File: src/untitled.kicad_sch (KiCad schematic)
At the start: 45 parts, among them J4 Conn_02x15_Odd_Even, J5 USB_C_Receptacle_USB2.0_14P, U4 W25Q128JVS, U5 NCP1117-1.5_SOT223, Y2 ABM8-272-T3

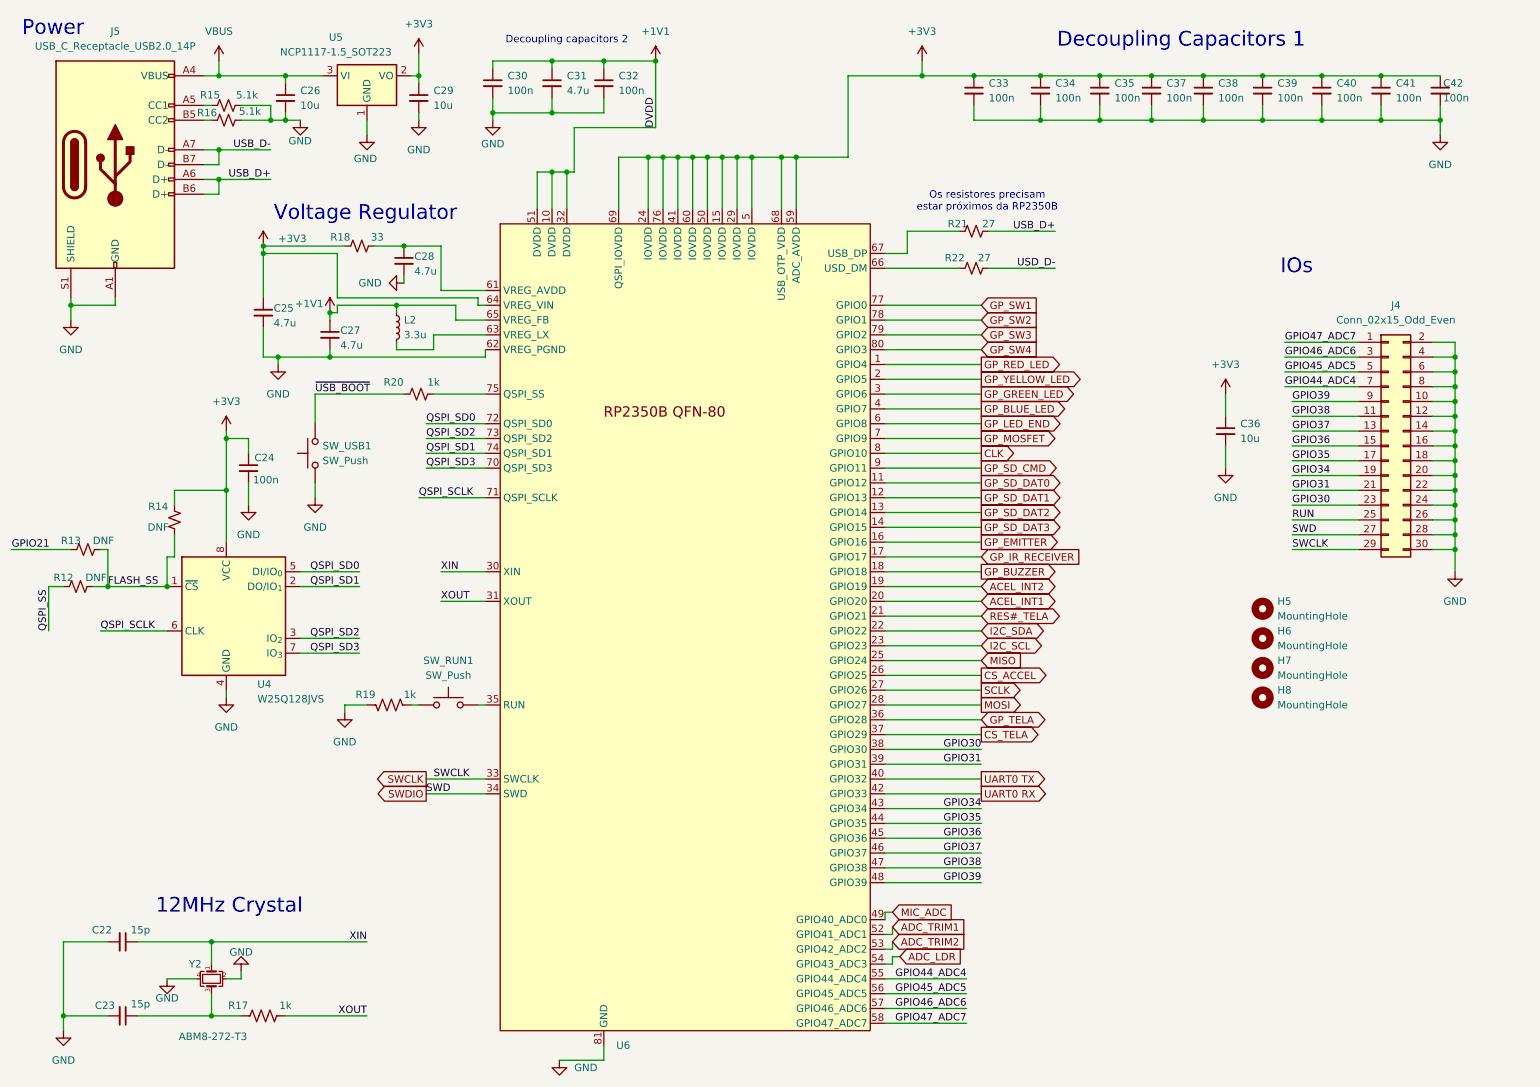
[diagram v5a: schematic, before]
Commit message: adicionado footprints, falta microfone e display somente
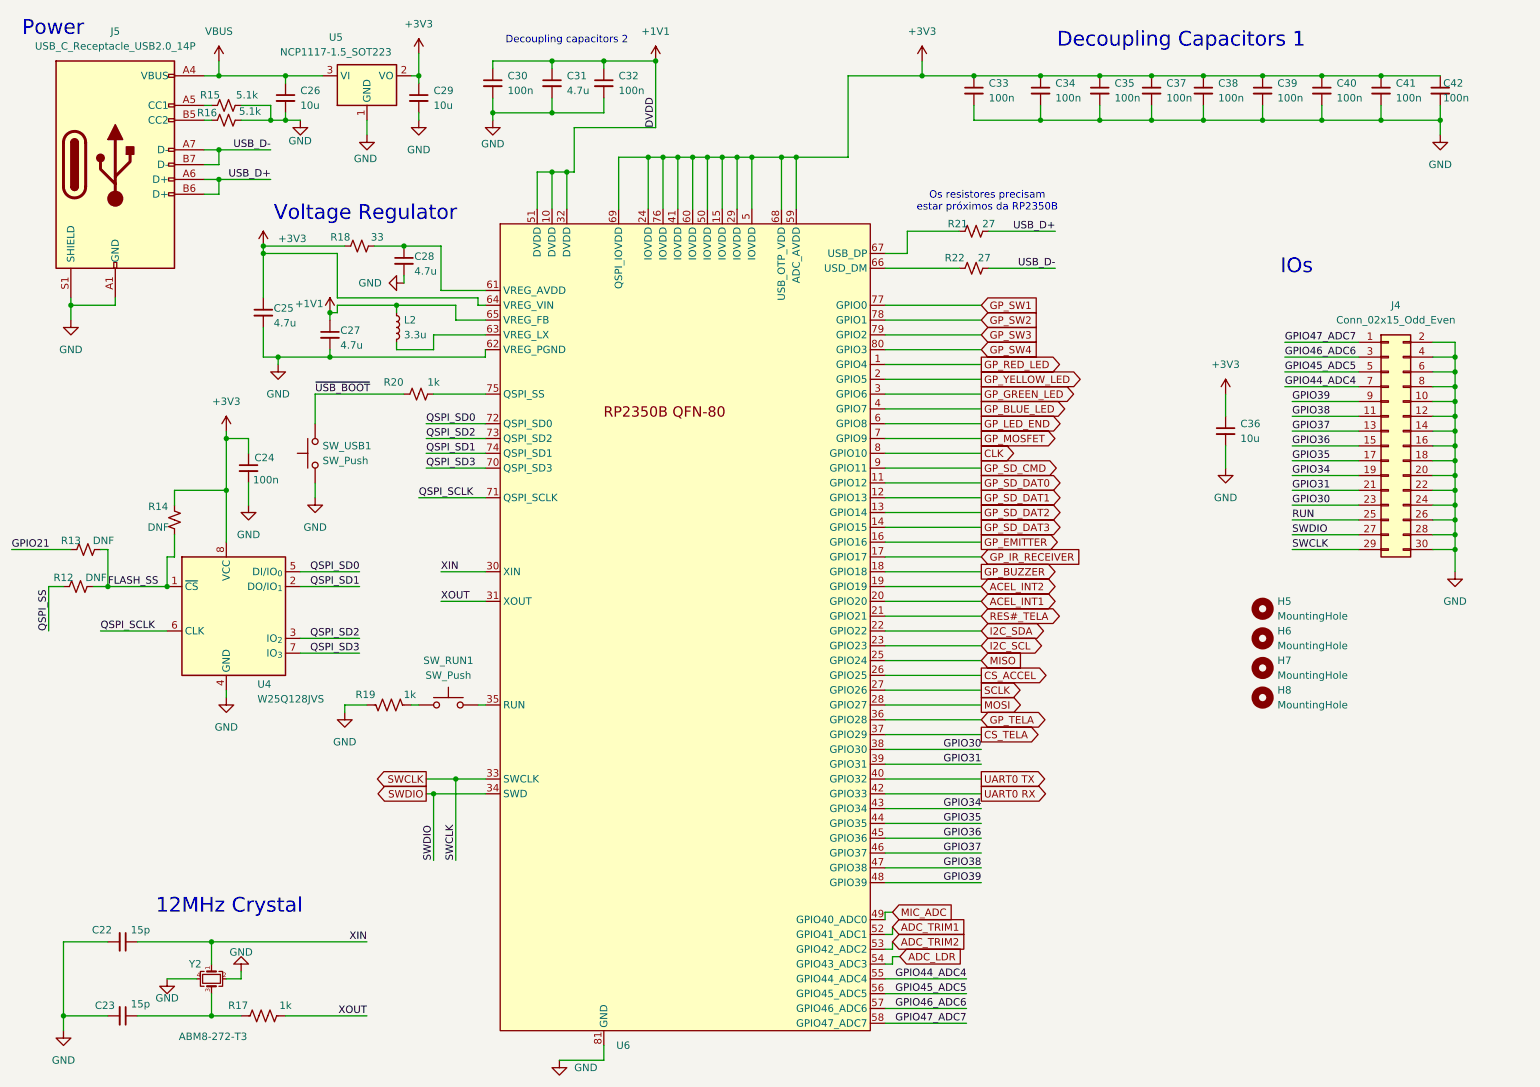
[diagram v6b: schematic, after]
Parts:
- H5, H6, H7, H8: footprint (none) -> MountingHole:MountingHole_2.2mm_M2
- R12, R13, R14, R21, R22: footprint (none) -> Resistor_SMD:R_0402_1005Metric
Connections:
- net USD_D- is gone; now on net USB_D-: R22.2
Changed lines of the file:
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@@
 	)
 	(junction
+		(at 85.09 147.32)
+		(diameter 0)
+		(color 0 0 0 0)
+	)
+	(junction
 		(at 48.26 24.13)
 		(diameter 0)
@@
 	)
 	(junction
+		(at 88.9 144.78)
+		(diameter 0)
+		(color 0 0 0 0)
+	)
+	(junction
 		(at 132.08 38.1)
 		(diameter 0)
@@
 	(wire
 		(pts
-			(xy 83.82 144.78) (xy 93.98 144.78)
+			(xy 83.82 144.78) (xy 88.9 144.78)
 		)
 		(stroke
@@
 	(wire
 		(pts
-			(xy 83.82 147.32) (xy 93.98 147.32)
+			(xy 83.82 147.32) (xy 85.09 147.32)
 		)
 		(stroke
@@
 	(wire
 		(pts
+			(xy 85.09 147.32) (xy 93.98 147.32)
+		)
+		(stroke
+			(width 0)
+			(type default)
+		)
+	)
+	(wire
+		(pts
 			(xy 52.07 29.21) (xy 57.15 29.21)
 		)
@@
 	(wire
 		(pts
+			(xy 88.9 144.78) (xy 93.98 144.78)
+		)
+		(stroke
+			(width 0)
+			(type default)
+		)
+	)
+	(wire
+		(pts
 			(xy 179.07 134.62) (xy 162.56 134.62)
 		)
@@
 	(wire
 		(pts
+			(xy 88.9 144.78) (xy 88.9 158.75)
+		)
+		(stroke
+			(width 0)
+			(type default)
+		)
+	)
+	(wire
+		(pts
 			(xy 162.56 81.28) (xy 179.07 81.28)
 		)
@@
 	(wire
 		(pts
+			(xy 85.09 147.32) (xy 85.09 158.75)
+		)
+		(stroke
+			(width 0)
+			(type default)
+		)
+	)
+	(wire
+		(pts
 			(xy 95.25 21.59) (xy 95.25 22.86)
 		)
@@
 		)
 	)
+	(label "SWCLK"
+		(at 88.9 158.75 90)
+		(effects
+			(font
+				(size 1.27 1.27)
+			)
+			(justify left bottom)
+		)
+	)
 	(label "GPIO34"
 		(at 179.07 149.86 180)
@@
 		)
 	)
-	(label "SWD"
-		(at 83.82 147.32 0)
-		(effects
-			(font
-				(size 1.27 1.27)
-			)
-			(justify left bottom)
-		)
-	)
 	(label "GPIO38"
 		(at 232.41 82.55 0)
@@
 		)
 	)
-	(label "SWCLK"
-		(at 85.09 144.78 0)
+	(label "SWDIO"
+		(at 85.09 158.75 90)
 		(effects
 			(font
@@
 		)
 	)
-	(label "SWD"
+	(label "SWDIO"
 		(at 232.41 102.87 0)
 		(effects
@@
 		)
 	)
-	(label "USD_D-"
+	(label "USB_D-"
 		(at 191.77 57.15 180)
 		(effects
@@
 			)
 		)
-		(property "Footprint" ""
+		(property "Footprint" "MountingHole:MountingHole_2.2mm_M2"
 			(at 227.33 130.81 0)
 			(effects
@@
 			)
 		)
-		(property "Footprint" ""
+		(property "Footprint" "Resistor_SMD:R_0402_1005Metric"
 			(at 24.13 111.76 0)
 			(effects
@@
 			)
 		)
-		(property "Footprint" ""
+		(property "Footprint" "Resistor_SMD:R_0402_1005Metric"
 			(at 177.8 50.8 0)
 			(effects
@@
 			)
 		)
-		(property "Footprint" ""
+		(property "Footprint" "MountingHole:MountingHole_2.2mm_M2"
 			(at 227.33 115.57 0)
 			(effects
@@
 			)
 		)
-		(property "Footprint" ""
+		(property "Footprint" "MountingHole:MountingHole_2.2mm_M2"
 			(at 227.33 125.73 0)
 			(effects
@@
 			)
 		)
-		(property "Footprint" ""
+		(property "Footprint" "MountingHole:MountingHole_2.2mm_M2"
 			(at 227.33 120.65 0)
 			(effects
@@
 			)
 		)
-		(property "Footprint" ""
+		(property "Footprint" "Resistor_SMD:R_0402_1005Metric"
 			(at 40.64 100.33 0)
 			(effects
@@
 			)
 		)
-		(property "Footprint" ""
+		(property "Footprint" "Resistor_SMD:R_0402_1005Metric"
 			(at 177.8 57.15 0)
 			(effects
@@
 			)
 		)
-		(property "Footprint" ""
+		(property "Footprint" "Resistor_SMD:R_0402_1005Metric"
 			(at 25.4 105.41 0)
 			(effects

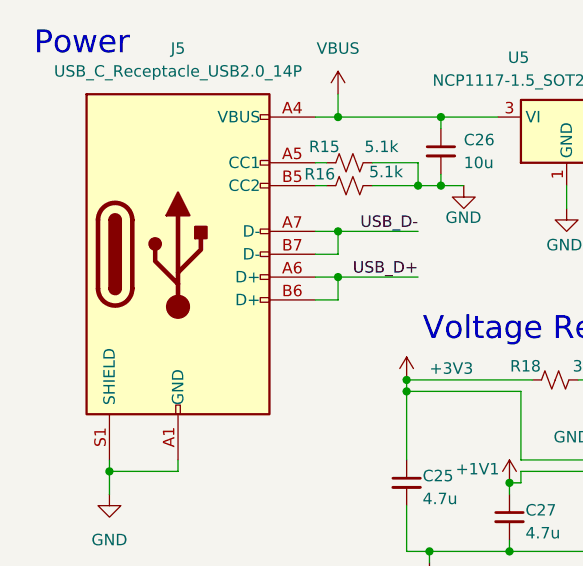
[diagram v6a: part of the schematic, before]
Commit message: Bugs na att da PCI resolvidos (falta só a tela OLED)
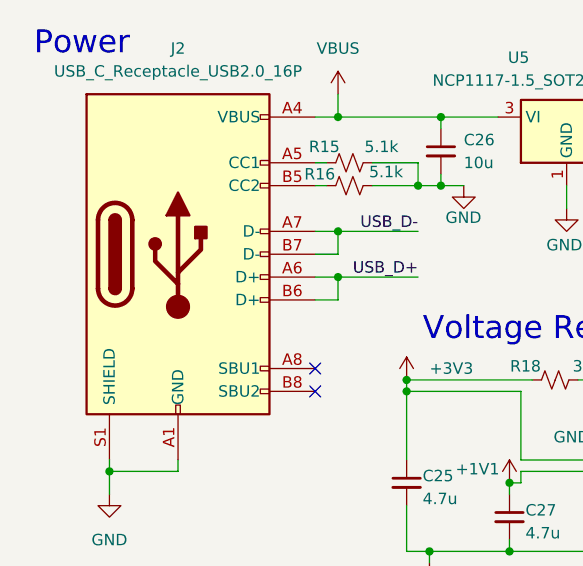
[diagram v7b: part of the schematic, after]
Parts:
- removed J5: USB_C_Receptacle_USB2.0_14P, Connector_USB:USB_C_Receptacle_GCT_USB4105-xx-A_16P_TopMnt_Horizontal, symbol Connector:USB_C_Receptacle_USB2.0_14P
- added J2: USB_C_Receptacle_USB2.0_16P, Connector_USB:USB_C_Receptacle_GCT_USB4105-xx-A_16P_TopMnt_Horizontal, symbol Connector:USB_C_Receptacle_USB2.0_16P
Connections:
- net GND: now also J2.A1 (GND), J2.A12 (GND), J2.B1 (GND), J2.B12 (GND), J2.S1 (SHIELD)
- net USB_D+: now also J2.A6 (D+), J2.B6 (D+)
- net USB_D-: now also J2.A7 (D-), J2.B7 (D-)
- net VBUS: now also J2.A4 (VBUS), J2.A9 (VBUS), J2.B4 (VBUS), J2.B9 (VBUS)
- net at R15.2: now also J2.A5 (CC1)
- net at R16.2: now also J2.B5 (CC2)
- no-connect marks 0 -> 2
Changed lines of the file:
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@@
 		(color 0 0 0 0)
 	)
+	(no_connect
+		(at 45.72 52.07)
+	)
+	(no_connect
+		(at 45.72 54.61)
+	)
 	(wire
 		(pts
@@
 	)
 	(symbol
-		(lib_id "Connector:USB_C_Receptacle_USB2.0_14P")
-		(at 30.48 39.37 0)
-		(unit 1)
-		(exclude_from_sim no)
-		(in_bom yes)
-		(on_board yes)
-		(dnp no)
-		(fields_autoplaced yes)
-		(property "Reference" "J5"
-			(at 30.48 16.51 0)
-			(effects
-				(font
-					(size 1.27 1.27)
-				)
-			)
-		)
-		(property "Value" "USB_C_Receptacle_USB2.0_14P"
-			(at 30.48 19.05 0)
-			(effects
-				(font
-					(size 1.27 1.27)
-				)
-			)
-		)
-		(property "Footprint" "Connector_USB:USB_C_Receptacle_GCT_USB4105-xx-A_16P_TopMnt_Horizontal"
-			(at 34.29 39.37 0)
-			(effects
-				(font
-					(size 1.27 1.27)
-				)
-				(hide yes)
-			)
-		)
-		(property "Datasheet" "https://www.usb.org/sites/default/files/documents/usb_type-c.zip"
-			(at 34.29 39.37 0)
-			(effects
-				(font
-					(size 1.27 1.27)
-				)
-				(hide yes)
-			)
-		)
-		(property "Description" "USB 2.0-only 14P Type-C Receptacle connector"
-			(at 30.48 39.37 0)
-			(effects
-				(font
-					(size 1.27 1.27)
-				)
-				(hide yes)
-			)
-		)
-		(pin "A6"
-		)
-		(pin "S1"
-		)
-		(pin "A12"
-		)
-		(pin "A4"
-		)
-		(pin "A5"
-		)
-		(pin "B1"
-		)
-		(pin "B5"
-		)
-		(pin "A1"
-		)
-		(pin "B4"
-		)
-		(pin "A7"
-		)
-		(pin "B12"
-		)
-		(pin "B9"
-		)
-		(pin "A9"
-		)
-		(pin "B7"
-		)
-		(pin "B6"
-		)
-		(instances
-			(project "Circuitos Impressos"
-				(path "/49caf936-61f8-45e5-bebd-98db7502d055/c83c4fed-140a-443e-a6d8-37ea998d1cae"
-					(reference "J5")
-					(unit 1)
-				)
-			)
-		)
-	)
-	(symbol
 		(lib_id "Switch:SW_Push")
 		(at 64.77 88.9 90)
@@
 					(unit 1)
 				)
+			)
+		)
+	)
+	(symbol
+		(lib_id "Connector:USB_C_Receptacle_USB2.0_16P")
+		(at 30.48 39.37 0)
+		(unit 1)
+		(exclude_from_sim no)
+		(in_bom yes)
+		(on_board yes)
+		(dnp no)
+		(fields_autoplaced yes)
+		(property "Reference" "J2"
+			(at 30.48 16.51 0)
+			(effects
+				(font
+					(size 1.27 1.27)
+				)
+			)
+		)
+		(property "Value" "USB_C_Receptacle_USB2.0_16P"
+			(at 30.48 19.05 0)
+			(effects
+				(font
+					(size 1.27 1.27)
+				)
+			)
+		)
+		(property "Footprint" "Connector_USB:USB_C_Receptacle_GCT_USB4105-xx-A_16P_TopMnt_Horizontal"
+			(at 34.29 39.37 0)
+			(effects
+				(font
+					(size 1.27 1.27)
+				)
+				(hide yes)
+			)
+		)
+		(property "Datasheet" "https://www.usb.org/sites/default/files/documents/usb_type-c.zip"
+			(at 34.29 39.37 0)
+			(effects
+				(font
+					(size 1.27 1.27)
+				)
+				(hide yes)
+			)
+		)
+		(property "Description" "USB 2.0-only 16P Type-C Receptacle connector"
+			(at 30.48 39.37 0)
+			(effects
+				(font
+					(size 1.27 1.27)
+				)
+				(hide yes)
+			)
+		)
+		(pin "B9"
+		)
+		(pin "A7"
+		)
+		(pin "A8"
+		)
+		(pin "B8"
+		)
+		(pin "B4"
+		)
+		(pin "A5"
+		)
+		(pin "A12"
+		)
+		(pin "B6"
+		)
+		(pin "A4"
+		)
+		(pin "S1"
+		)
+		(pin "B1"
+		)
+		(pin "B7"
+		)
+		(pin "A1"
+		)
+		(pin "B12"
+		)
+		(pin "A9"
+		)
+		(pin "B5"
+		)
+		(pin "A6"
+		)
+		(instances
+			(project ""
+				(path "/49caf936-61f8-45e5-bebd-98db7502d055/c83c4fed-140a-443e-a6d8-37ea998d1cae"
+					(reference "J2")
+					(unit 1)
+				)

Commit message: placement finalizado, faltando trilhas
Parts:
- SW_USB1: footprint Button_Switch_SMD:SW_Push_1P1T_NO_CK_PTS125Sx43PSMTR -> Button_Switch_SMD:SW_Tactile_SPST_NO_Straight_CK_PTS636Sx25SMTRLFS
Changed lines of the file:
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@@
 			)
 		)
-		(property "Footprint" "Button_Switch_SMD:SW_Push_1P1T_NO_CK_PTS125Sx43PSMTR"
+		(property "Footprint" "Button_Switch_SMD:SW_Tactile_SPST_NO_Straight_CK_PTS636Sx25SMTRLFS"
 			(at 59.69 88.9 0)
 			(effects
